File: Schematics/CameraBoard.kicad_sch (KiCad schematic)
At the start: 0 parts

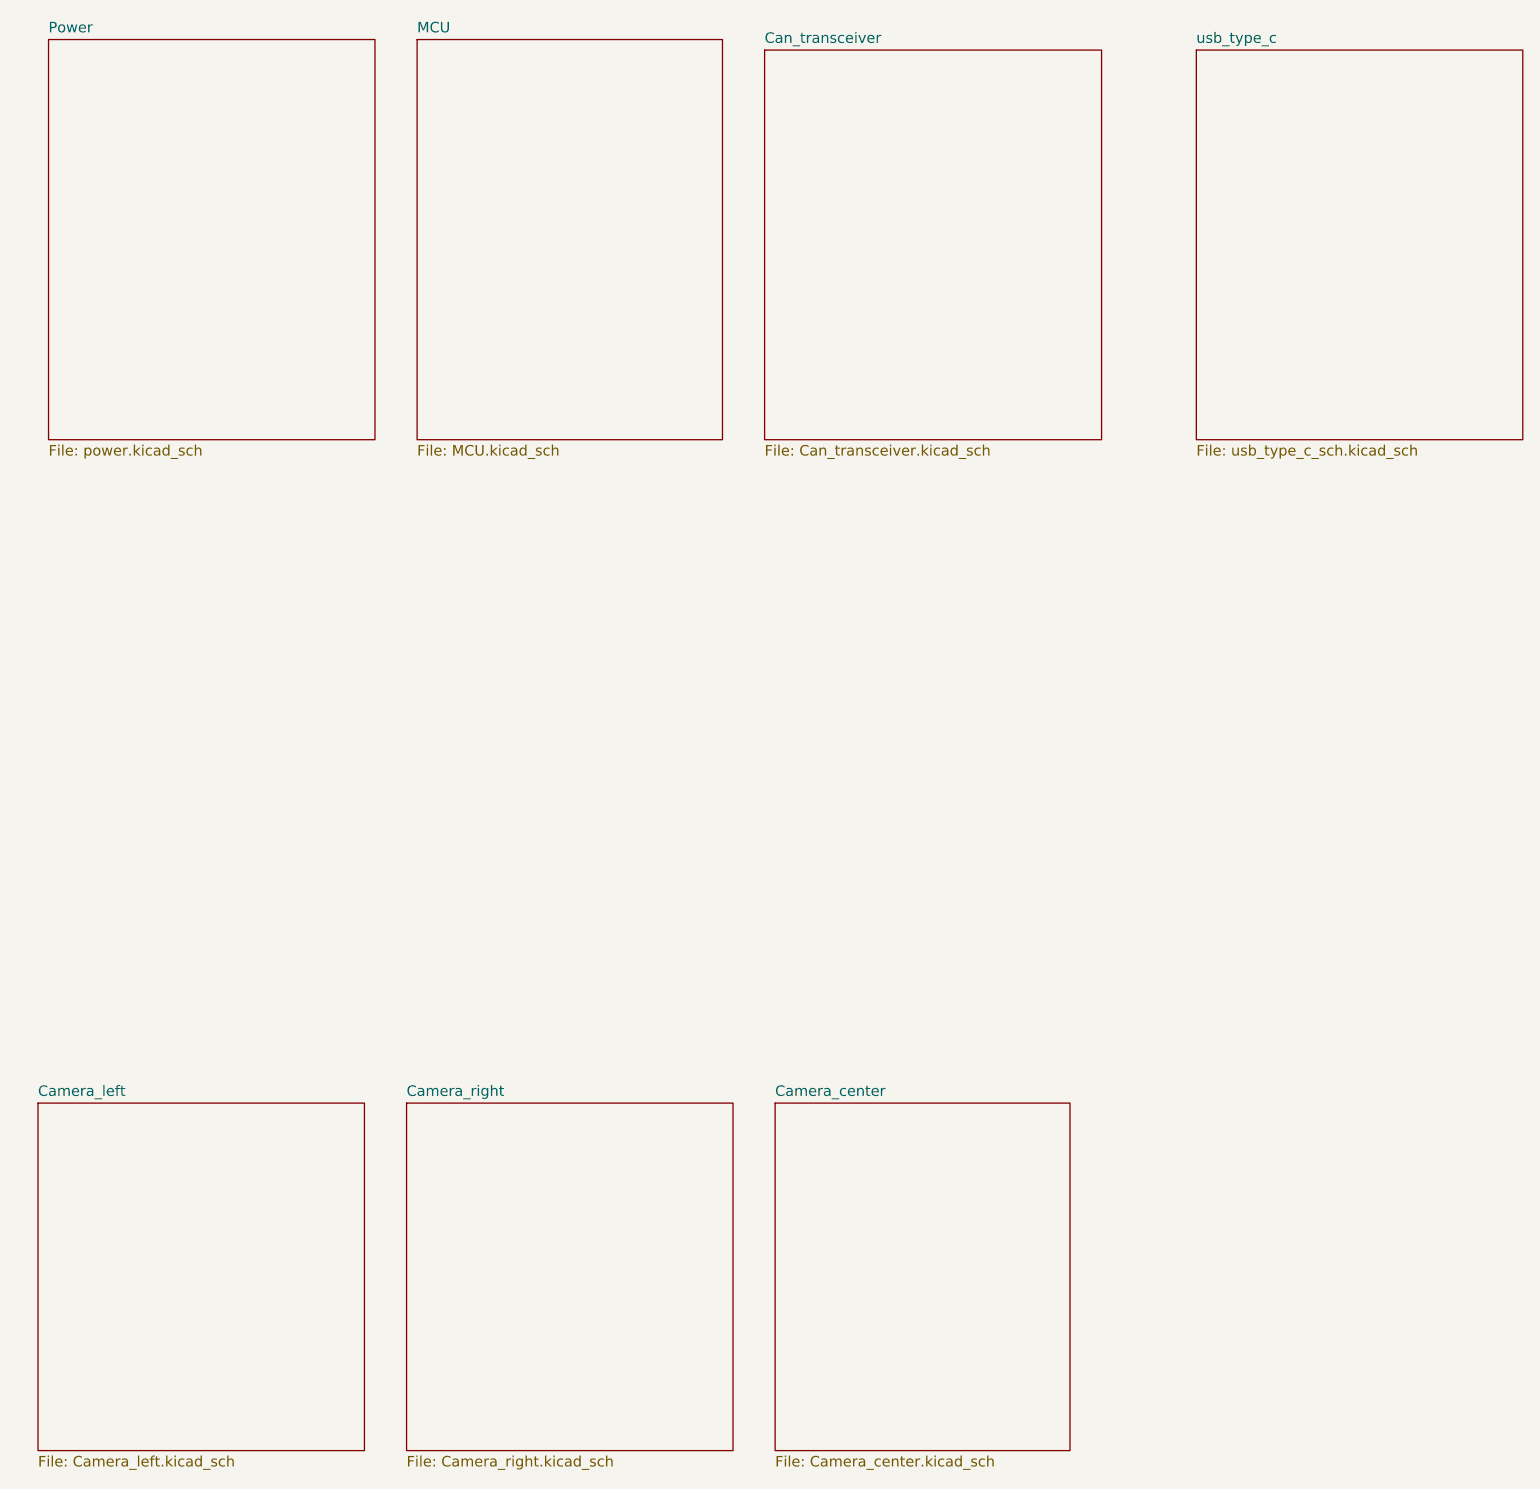
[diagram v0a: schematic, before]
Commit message: second final draft finished routing added swd debug with stlink capabilities pending review for and data sheet review to ensure parts are correct, also need to edge cut ocillator
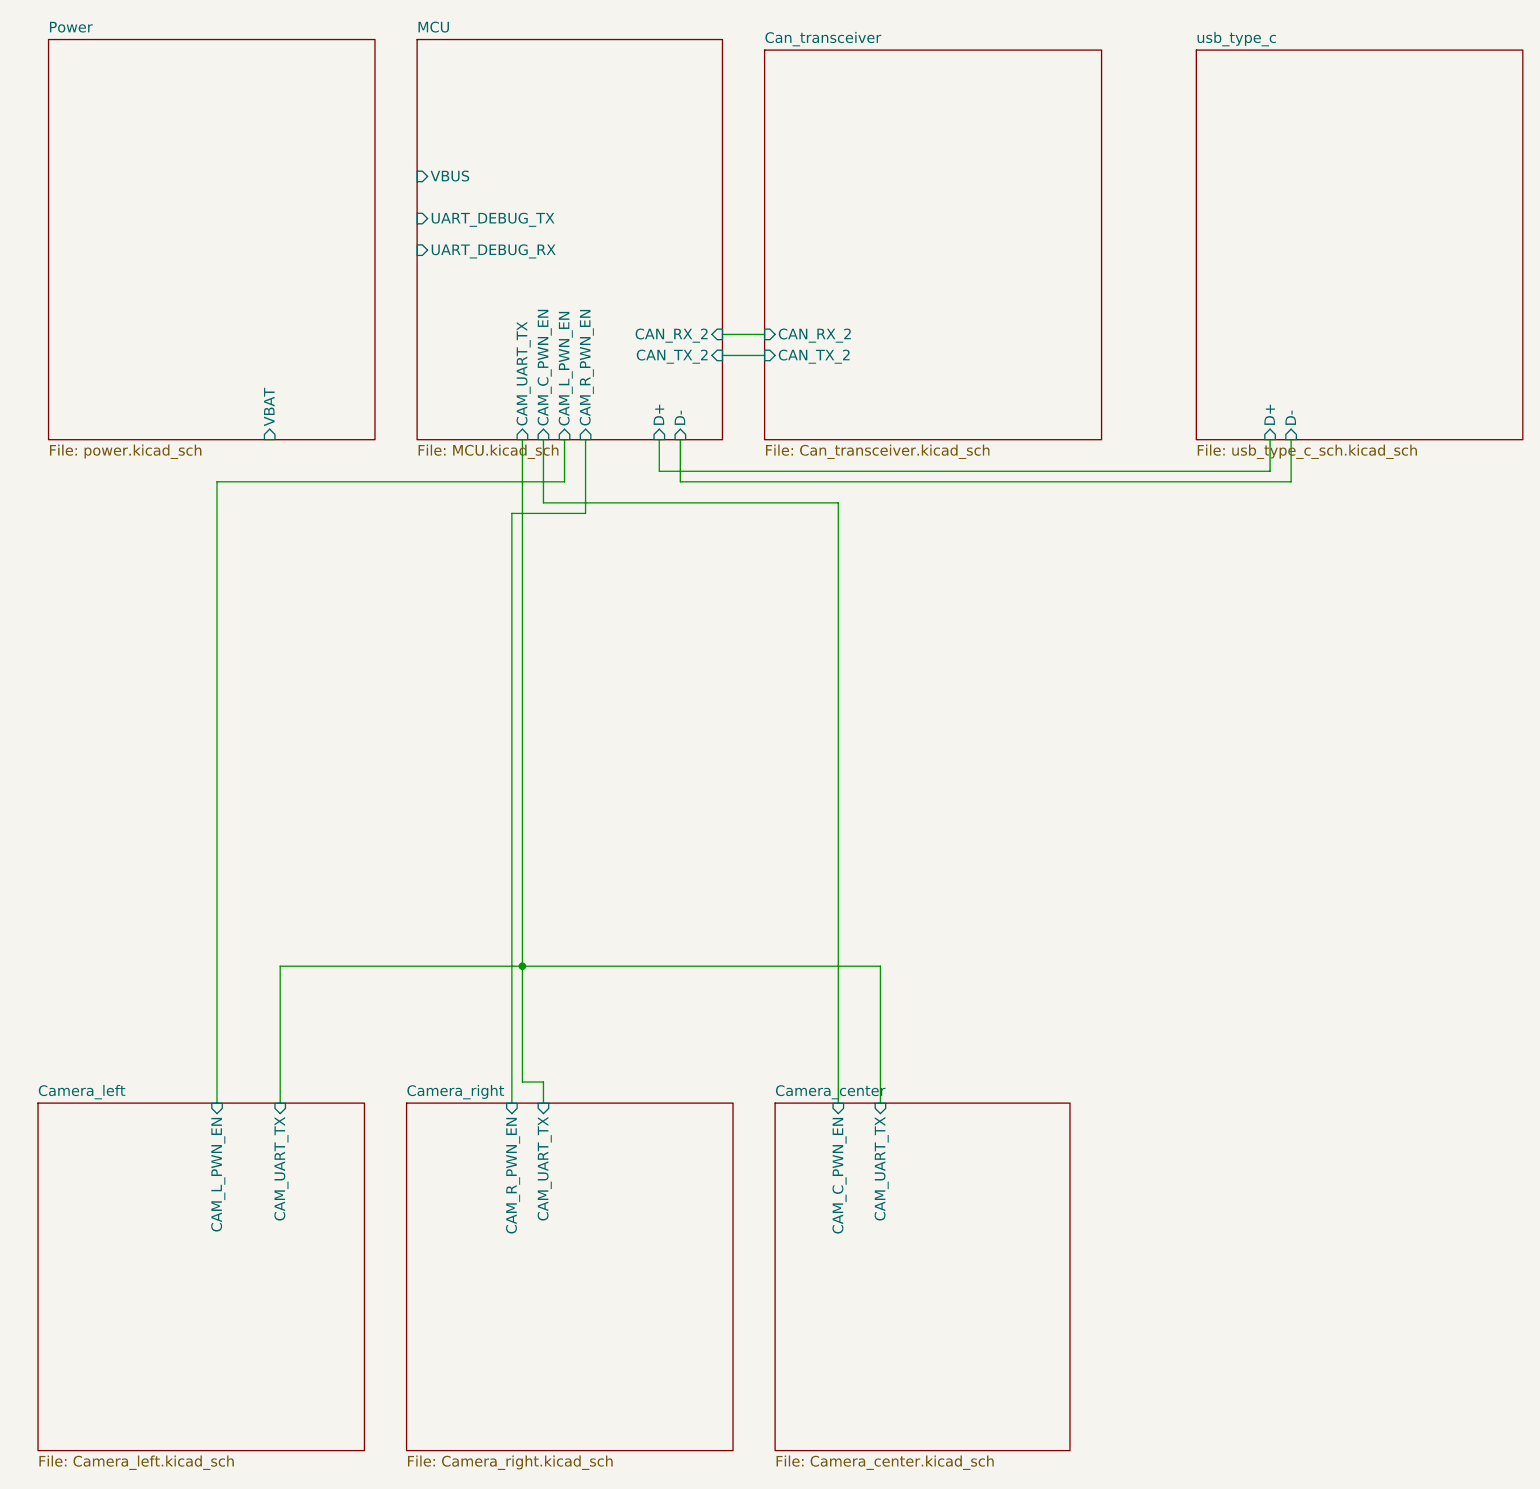
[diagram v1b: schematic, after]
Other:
- sheet Camera_center ports: added CAM_C_PWN_EN, CAM_UART_TX; removed none
- sheet Camera_left ports: added CAM_L_PWN_EN, CAM_UART_TX; removed none
- sheet Camera_right ports: added CAM_R_PWN_EN, CAM_UART_TX; removed none
- sheet Can_transceiver ports: added CAN_RX_2, CAN_TX_2; removed none
- sheet MCU ports: added CAM_C_PWN_EN, CAM_L_PWN_EN, CAM_R_PWN_EN, CAM_UART_TX, CAN_RX_2, CAN_TX_2, D+, D-, UART_DEBUG_RX, UART_DEBUG_TX, VBUS; removed none
- sheet Power ports: added VBAT; removed none
- sheet usb_type_c ports: added D+, D-; removed none

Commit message: added LCSC numbers and generated BOM, fixed schematic
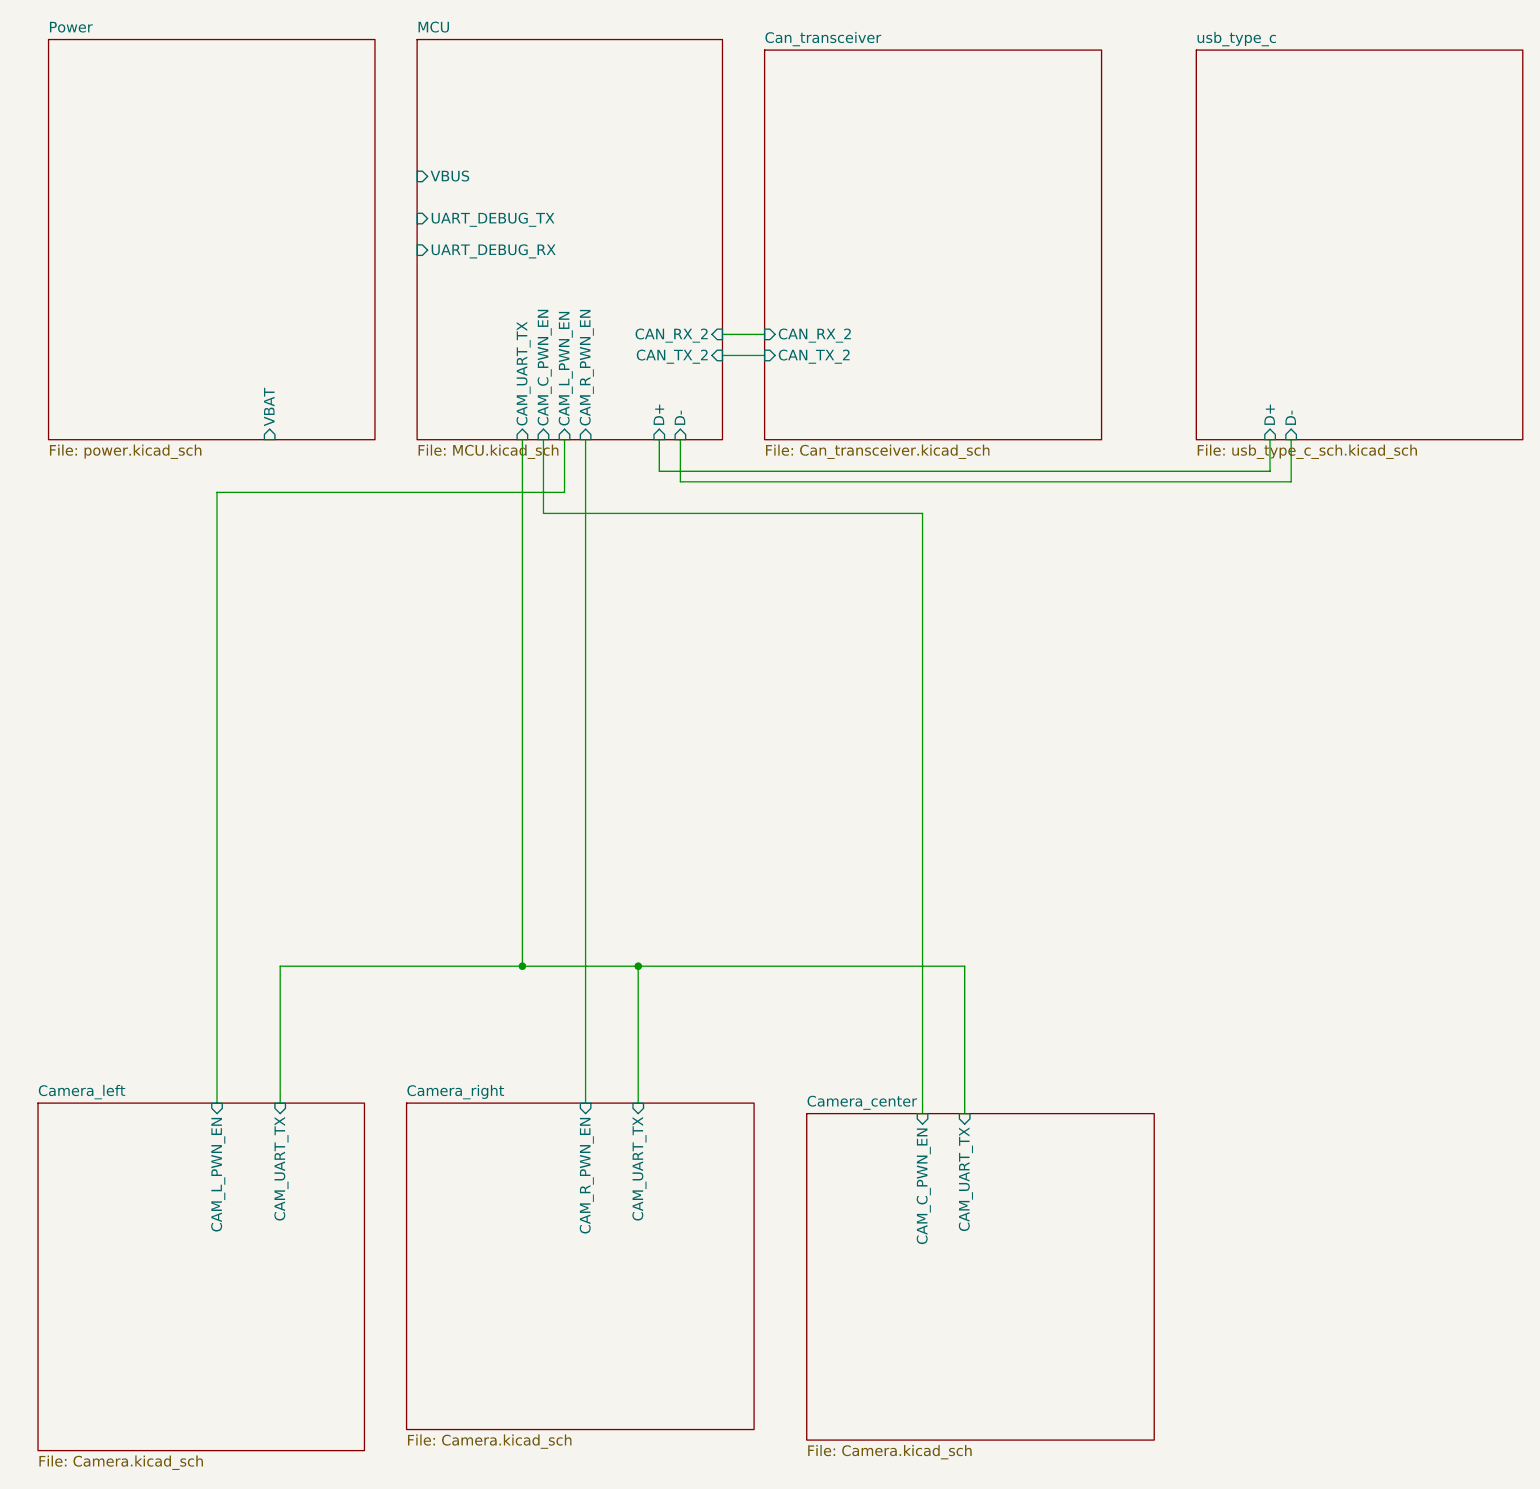
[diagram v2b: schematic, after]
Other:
- sheet Camera_center: file Camera_center.kicad_sch -> Camera.kicad_sch
- sheet Camera_left: file Camera_left.kicad_sch -> Camera.kicad_sch
- sheet Camera_right: file Camera_right.kicad_sch -> Camera.kicad_sch
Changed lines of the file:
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@@
 	(paper "A4")
+	(junction
+		(at 91.44 129.54)
+		(diameter 0)
+		(color 0 0 0 0)
+	)
 	(junction
 		(at 77.47 129.54)
@@
 	(wire
 		(pts
-			(xy 40.64 146.05) (xy 40.64 71.12)
-		)
-		(stroke
-			(width 0)
-			(type default)
-		)
-	)
-	(wire
-		(pts
-			(xy 40.64 71.12) (xy 82.55 71.12)
-		)
-		(stroke
-			(width 0)
-			(type default)
-		)
-	)
-	(wire
-		(pts
 			(xy 170.18 66.04) (xy 170.18 71.12)
 		)
@@
 	(wire
 		(pts
+			(xy 77.47 129.54) (xy 91.44 129.54)
+		)
+		(stroke
+			(width 0)
+			(type default)
+		)
+	)
+	(wire
+		(pts
 			(xy 170.18 71.12) (xy 96.52 71.12)
 		)
@@
 	(wire
 		(pts
-			(xy 80.01 73.66) (xy 80.01 66.04)
+			(xy 85.09 66.04) (xy 85.09 146.05)
 		)
 		(stroke
@@
 	(wire
 		(pts
+			(xy 125.73 147.32) (xy 125.73 74.93)
+		)
+		(stroke
+			(width 0)
+			(type default)
+		)
+	)
+	(wire
+		(pts
 			(xy 96.52 71.12) (xy 96.52 66.04)
 		)
@@
 	(wire
 		(pts
-			(xy 76.2 74.93) (xy 85.09 74.93)
-		)
-		(stroke
-			(width 0)
-			(type default)
-		)
-	)
-	(wire
-		(pts
-			(xy 120.65 129.54) (xy 120.65 146.05)
+			(xy 91.44 129.54) (xy 130.81 129.54)
 		)
 		(stroke
@@
 	(wire
 		(pts
-			(xy 80.01 143.51) (xy 80.01 146.05)
-		)
-		(stroke
-			(width 0)
-			(type default)
-		)
-	)
-	(wire
-		(pts
-			(xy 115.57 146.05) (xy 115.57 73.66)
-		)
-		(stroke
-			(width 0)
-			(type default)
-		)
-	)
-	(wire
-		(pts
-			(xy 115.57 73.66) (xy 80.01 73.66)
-		)
-		(stroke
-			(width 0)
-			(type default)
-		)
-	)
-	(wire
-		(pts
-			(xy 77.47 143.51) (xy 80.01 143.51)
-		)
-		(stroke
-			(width 0)
-			(type default)
-		)
-	)
-	(wire
-		(pts
-			(xy 85.09 74.93) (xy 85.09 66.04)
-		)
-		(stroke
-			(width 0)
-			(type default)
-		)
-	)
-	(wire
-		(pts
-			(xy 77.47 129.54) (xy 120.65 129.54)
+			(xy 40.64 72.39) (xy 82.55 72.39)
+		)
+		(stroke
+			(width 0)
+			(type default)
+		)
+	)
+	(wire
+		(pts
+			(xy 82.55 72.39) (xy 82.55 66.04)
+		)
+		(stroke
+			(width 0)
+			(type default)
+		)
+	)
+	(wire
+		(pts
+			(xy 40.64 146.05) (xy 40.64 72.39)
+		)
+		(stroke
+			(width 0)
+			(type default)
+		)
+	)
+	(wire
+		(pts
+			(xy 125.73 74.93) (xy 80.01 74.93)
+		)
+		(stroke
+			(width 0)
+			(type default)
+		)
+	)
+	(wire
+		(pts
+			(xy 80.01 74.93) (xy 80.01 66.04)
 		)
 		(stroke
@@
 	(wire
 		(pts
+			(xy 91.44 146.05) (xy 91.44 129.54)
+		)
+		(stroke
+			(width 0)
+			(type default)
+		)
+	)
+	(wire
+		(pts
 			(xy 101.6 55.88) (xy 106.68 55.88)
 		)
@@
 	(wire
 		(pts
-			(xy 82.55 71.12) (xy 82.55 66.04)
-		)
-		(stroke
-			(width 0)
-			(type default)
-		)
-	)
-	(wire
-		(pts
-			(xy 76.2 146.05) (xy 76.2 74.93)
-		)
-		(stroke
-			(width 0)
-			(type default)
-		)
-	)
-	(wire
-		(pts
-			(xy 77.47 129.54) (xy 77.47 143.51)
-		)
-		(stroke
-			(width 0)
-			(type default)
+			(xy 130.81 129.54) (xy 130.81 147.32)
+		)
+		(stroke
+			(width 0)
+			(type default)
+		)
+	)
+	(sheet
+		(at 111.76 147.32)
+		(size 41.91 39.37)
+		(exclude_from_sim no)
+		(in_bom yes)
+		(on_board yes)
+		(dnp no)
+		(fields_autoplaced yes)
+		(stroke
+			(width 0.1524)
+			(type solid)
+		)
+		(fill
+			(color 0 0 0 0.0000)
+		)
+		(property "Sheetname" "Camera_center"
+			(at 111.76 146.6084 0)
+			(effects
+				(font
+					(size 1.27 1.27)
+				)
+				(justify left bottom)
+			)
+		)
+		(property "Sheetfile" "Camera.kicad_sch"
+			(at 111.76 187.2746 0)
+			(effects
+				(font
+					(size 1.27 1.27)
+				)
+				(justify left top)
+			)
+		)
+		(pin "CAM_C_PWN_EN" input
+			(at 125.73 147.32 90)
+			(effects
+				(font
+					(size 1.27 1.27)
+				)
+				(justify right)
+			)
+		)
+		(pin "CAM_UART_TX" input
+			(at 130.81 147.32 90)
+			(effects
+				(font
+					(size 1.27 1.27)
+				)
+				(justify right)
+			)
+		)
+		(instances
+			(project "CameraBoard"
+				(path "/65068a32-f105-4204-b50e-234054c5a6d0"
+					(page "10")
+				)
+			)
 		)
 	)
@@
 	)
 	(sheet
-		(at 107.95 146.05)
-		(size 35.56 41.91)
+		(at 63.5 146.05)
+		(size 41.91 39.37)
 		(exclude_from_sim no)
 		(in_bom yes)
@@
 			(color 0 0 0 0.0000)
 		)
-		(property "Sheetname" "Camera_center"
-			(at 107.95 145.3384 0)
+		(property "Sheetname" "Camera_right"
+			(at 63.5 145.3384 0)
 			(effects
 				(font
@@
 			)
 		)
-		(property "Sheetfile" "Camera_center.kicad_sch"
-			(at 107.95 188.5446 0)
+		(property "Sheetfile" "Camera.kicad_sch"
+			(at 63.5 186.0046 0)
 			(effects
 				(font
@@
 			)
 		)
-		(pin "CAM_C_PWN_EN" input
-			(at 115.57 146.05 90)
+		(pin "CAM_R_PWN_EN" input
+			(at 85.09 146.05 90)
 			(effects
 				(font
@@
 		)
 		(pin "CAM_UART_TX" input
-			(at 120.65 146.05 90)
+			(at 91.44 146.05 90)
 			(effects
 				(font
@@
 			(project "CameraBoard"
 				(path "/65068a32-f105-4204-b50e-234054c5a6d0"
-					(page "6")
+					(page "9")
 				)
 			)
@@
 	)
 	(sheet
-		(at 63.5 146.05)
-		(size 39.37 41.91)
-		(exclude_from_sim no)
-		(in_bom yes)
-		(on_board yes)
-		(dnp no)
-		(fields_autoplaced yes)
-		(stroke
-			(width 0.1524)
-			(type solid)
-		)
-		(fill
-			(color 0 0 0 0.0000)
-		)
-		(property "Sheetname" "Camera_right"
-			(at 63.5 145.3384 0)
-			(effects
-				(font
-					(size 1.27 1.27)
-				)
-				(justify left bottom)
-			)
-		)
-		(property "Sheetfile" "Camera_right.kicad_sch"
-			(at 63.5 188.5446 0)
-			(effects
-				(font
-					(size 1.27 1.27)
-				)
-				(justify left top)
-			)
-		)
-		(pin "CAM_R_PWN_EN" input
-			(at 76.2 146.05 90)
-			(effects
-				(font
-					(size 1.27 1.27)
-				)
-				(justify right)
-			)
-		)
-		(pin "CAM_UART_TX" input
-			(at 80.01 146.05 90)
-			(effects
-				(font
-					(size 1.27 1.27)
-				)
-				(justify right)
-			)
-		)
-		(instances
-			(project "CameraBoard"
-				(path "/65068a32-f105-4204-b50e-234054c5a6d0"
-					(page "5")
-				)
-			)
-		)
-	)
-	(sheet
 		(at 19.05 146.05)
 		(size 39.37 41.91)
@@
 			)
 		)
-		(property "Sheetfile" "Camera_left.kicad_sch"
+		(property "Sheetfile" "Camera.kicad_sch"
 			(at 19.05 188.5446 0)
 			(effects
